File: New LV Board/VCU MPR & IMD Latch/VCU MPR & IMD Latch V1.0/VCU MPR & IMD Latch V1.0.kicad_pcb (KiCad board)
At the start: 2 copper layers, 46.1 x 74.9 mm, 17 parts, among them J1 691137710002, J2 B12B-PH-K-S, J4 691137710002, J5 PH1-20-UA, J7 PH1-20-UA, K1 ALF1PF12, K2 AHES4291, SW1 Test Reset IMD

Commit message: VCU MPR & IMD Latch PCB
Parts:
- added K3: A161CS12VDC.64, Library:RELAY_A161CS12VDC.64, F.Cu at (77.9, 121.3)
- added K4: A161CS12VDC.64, Library:RELAY_A161CS12VDC.64, F.Cu at (78.1, 132.3)
- K2: value AHES4291 -> A161CS12VDC.64; footprint motorsports:AHES4_PAN -> Library:RELAY_A161CS12VDC.64
- moved K2 15.0 mm to (78.0, 112.4)
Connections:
- D1 pad 2: /GND -> Net-(D1-A)
- D2 pad 2: /GND -> Net-(D1-A)
- D3 pad 2: /GND -> Net-(D3-A)
- J2 pad 4: /Vs -> Net-(J2-Pad2)
- J2 pad 6: Net-(J2-Pad2) -> Net-(D3-A)
- J2 pad 7: /GND -> Net-(D1-A)
- R1 pad 1: /GND -> Net-(D1-A)
- R2 pad 1: /GND -> Net-(D1-A)
- R3 pad 2: /GND -> Net-(D1-A)
- SW1 pad 2: (no net) -> Net-(J2-Pad2)
- SW1 pad 4: Net-(J2-Pad2) -> (no net)
- TP2 pad 1: Net-(J2-Pad8) -> Net-(D1-A)
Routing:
- net Net-(D3-A): track 0.00 -> 165.9 mm
- net Net-(D1-K): track 74.7 -> 145.2 mm
- net /GND: track 67.8 -> 0.00 mm
- net (no net): track 0.00 -> 67.8 mm
- net Net-(J2-Pad2): track 78.6 -> 116.6 mm
- net /Vs: track 34.6 -> 0.00 mm
- net Net-(J4-Pad2): track 8.80 -> 20.5 mm
- net Net-(D1-A): track 0.00 -> 6.43 mm
- net Net-(D4-A): track 48.1 -> 49.0 mm

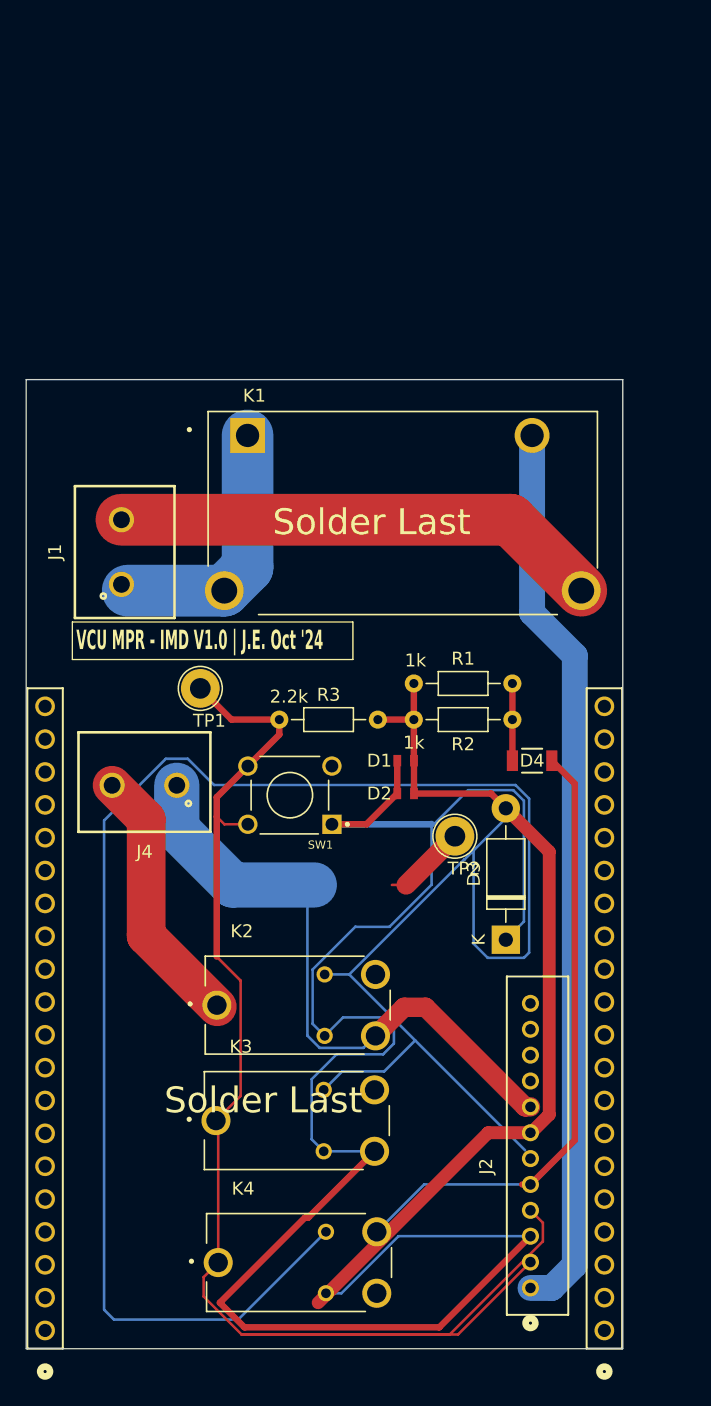
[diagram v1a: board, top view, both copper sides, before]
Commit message: Changed file name of VCU Throttle Latching to Throttle Latching Module, attempt to make VCU MPR & IMD Latch into IMD Latch & AMS Latch.
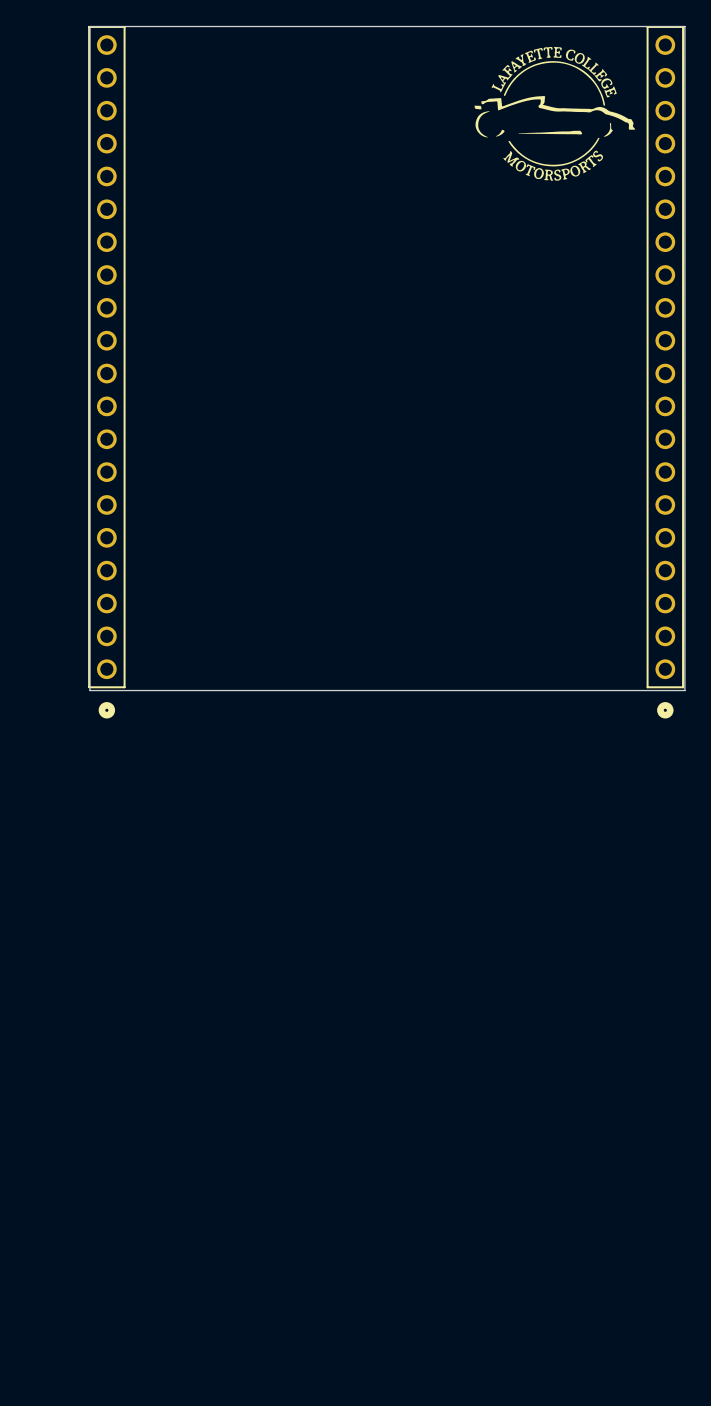
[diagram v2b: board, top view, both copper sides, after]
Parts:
- removed D1, D2: D_Zener, motorsports:STA_RMCF0603_STP-L
- removed D3: 1N4001, Diode_THT:D_DO-41_SOD81_P10.16mm_Horizontal
- removed D4: LED (Test), motorsports:LED_AP3216SYD_KNB
- removed J1, J4: 691137710002, motorsports:691137710002
- removed J2: B12B-PH-K-S, MotorSports_KICad:CONN12_B12B-PH_JST
- removed J5, J7: PH1-20-UA, PH1-20-UA:CONN_PH1-20-UA_ADM
- removed K1: ALF1PF12, motorsports:RELAY_ALF1PF12
- removed K2, K3, K4: A161CS12VDC.64, Library:RELAY_A161CS12VDC.64
- removed R1, R2: 1k, Resistor_THT:R_Axial_DIN0204_L3.6mm_D1.6mm_P7.62mm_Horizontal
- removed R3: 2.2k, Resistor_THT:R_Axial_DIN0204_L3.6mm_D1.6mm_P7.62mm_Horizontal
- removed SW1: Test Reset IMD, motorsports:pushButton
- removed TP1, TP2: TestPoint, TestPoint:TestPoint_Loop_D2.60mm_Drill1.6mm_Beaded
- added P1: PH1-20-UA, PH1-20-UA:CONN_PH1-20-UA_ADM, F.Cu at (106.4, 86.4)
- added P2: PH1-20-UA, PH1-20-UA:CONN_PH1-20-UA_ADM, F.Cu at (63.3, 86.4)
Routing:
- net Net-(D3-A): track 165.9 -> 0.00 mm
- net Net-(D1-K): track 145.2 -> 0.00 mm
- net Net-(J2-Pad2): track 116.6 -> 0.00 mm
- net Net-(J2-Pad1): track 69.7 -> 0.00 mm
- net (no net): track 67.8 -> 0.00 mm
- net Net-(J2-Pad8): track 49.8 -> 0.00 mm
- net Net-(D4-A): track 49.0 -> 0.00 mm
- net Net-(J1-Pad2): track 37.8 -> 0.00 mm
- net Net-(J1-Pad1): track 20.9 -> 0.00 mm
- net Net-(J4-Pad2): track 20.5 -> 0.00 mm
- net Net-(D1-A): track 6.43 -> 0.00 mm
- net Net-(D4-K): track 6.20 -> 0.00 mm
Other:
- board size 46.1 x 74.9 mm -> 46 x 51.3 mm
- board text removed: "Solder Last"
- board text removed: "VCU MPR - IMD V1.0 | J.E. Oct '24"

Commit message: AMS and IMD Latch combination
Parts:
- added D1: 1N4743A, Diode_THT:D_DO-41_SOD81_P3.81mm_Vertical_AnodeUp, F.Cu at (99.7, 58.4)
- added D2: 1N4743A, Diode_THT:D_DO-41_SOD81_P3.81mm_Vertical_AnodeUp, F.Cu at (99.7, 54.6)
- added D3: 1N4001, Diode_THT:D_DO-41_SOD81_P10.16mm_Horizontal, F.Cu at (82.8, 86.4)
- added D4: LED (Test), LED_THT:LED_D3.0mm, F.Cu at (85.2, 54.6)
- added D5: 1N4743A, Diode_THT:D_DO-41_SOD81_P3.81mm_Vertical_AnodeUp, F.Cu at (99.7, 50.8)
- added D6: 1N4743A, Diode_THT:D_DO-41_SOD81_P3.81mm_Vertical_AnodeUp, F.Cu at (99.7, 47.0)
- added D7: 1N4001, Diode_THT:D_DO-41_SOD81_P10.16mm_Horizontal, F.Cu at (66.3, 86.4)
- added D8: LED (Test), LED_THT:LED_D3.0mm, F.Cu at (68.7, 54.6)
- added J2: B12B-PH-K-S, Connector_JST:JST_PH_B12B-PH-K_1x12_P2.00mm_Vertical, F.Cu at (100.3, 85.1)
- added K1: A161CS12VDC.64, Library:RELAY_A161CS12VDC.64, F.Cu at (88.9, 80.2)
- added K2: A161CS12VDC.64, Library:RELAY_A161CS12VDC.64, F.Cu at (88.9, 62.0)
- added K3: A161CS12VDC.64, Library:RELAY_A161CS12VDC.64, F.Cu at (88.9, 71.1)
- added K4: A161CS12VDC.64, Library:RELAY_A161CS12VDC.64, F.Cu at (72.4, 80.0)
- added K5: A161CS12VDC.64, Library:RELAY_A161CS12VDC.64, F.Cu at (72.4, 62.2)
- added K6: A161CS12VDC.64, Library:RELAY_A161CS12VDC.64, F.Cu at (72.4, 71.1)
- added R1: 680, Resistor_THT:R_Axial_DIN0207_L6.3mm_D2.5mm_P2.54mm_Vertical, F.Cu at (85.1, 50.8)
- added R2: 680, Resistor_THT:R_Axial_DIN0207_L6.3mm_D2.5mm_P2.54mm_Vertical, F.Cu at (68.6, 50.8)
- added R3: 2.2k, Resistor_THT:R_Axial_DIN0207_L6.3mm_D2.5mm_P2.54mm_Vertical, F.Cu at (88.9, 55.3)
- added R4: 2.2k, Resistor_THT:R_Axial_DIN0207_L6.3mm_D2.5mm_P2.54mm_Vertical, F.Cu at (72.4, 55.3)
- added SW1: Test Reset IMD, motorsports:pushButton, F.Cu at (94.0, 52.2)
- added SW2: Test Reset IMD, motorsports:pushButton, F.Cu at (77.5, 52.2)
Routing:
- net Net-(D5-K): track 0.00 -> 103.4 mm
- net Net-(D1-A): track 0.00 -> 87.7 mm
- net Net-(D1-K): track 0.00 -> 80.8 mm
- net Net-(J2-Pad2): track 0.00 -> 69.5 mm
- net Net-(J2-Pad12): track 0.00 -> 68.7 mm
- net Net-(D7-A): track 0.00 -> 66.7 mm
- net Net-(J2-Pad4): track 0.00 -> 49.4 mm
- net Net-(D4-A): track 0.00 -> 39.1 mm
- net Net-(D8-A): track 0.00 -> 20.8 mm
- net Net-(J2-Pad1): track 0.00 -> 7.86 mm
- net Net-(K1-PadNO): track 0.00 -> 5.17 mm
- net Net-(D8-K): track 0.00 -> 4.90 mm
- net Net-(D4-K): track 0.00 -> 4.90 mm
